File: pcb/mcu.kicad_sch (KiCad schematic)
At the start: 15 parts, among them J2 Conn_01x07_Pin, J3 62201021121, SW2 SKRKAEE020, SW3 SKRKAEE020, U2 MS88SF2

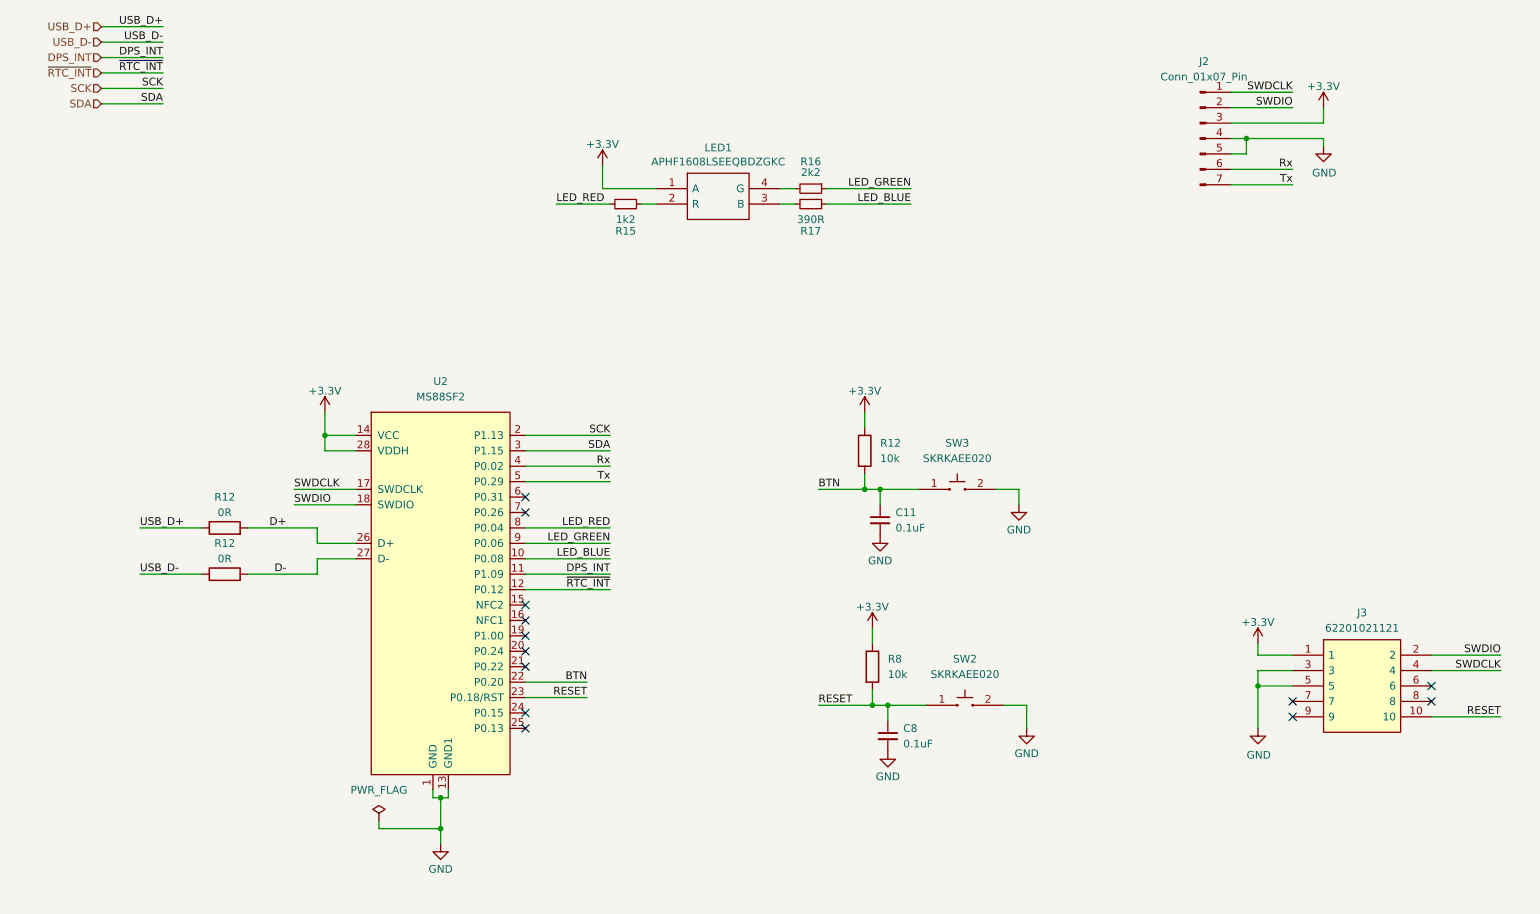
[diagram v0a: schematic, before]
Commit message: Replaces nRF52840 with ESP32-S3
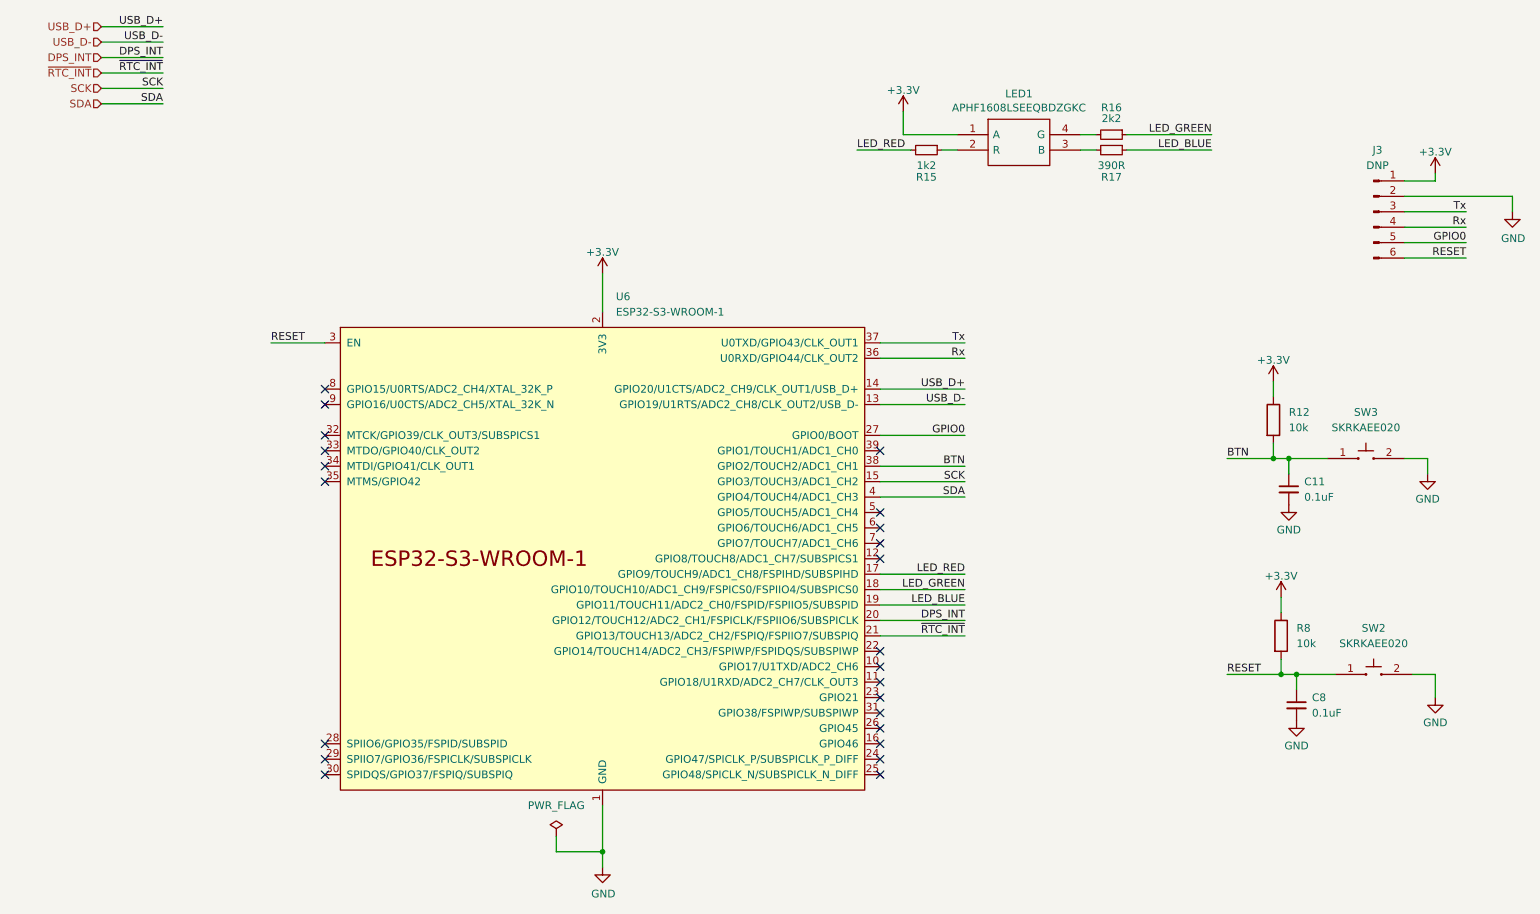
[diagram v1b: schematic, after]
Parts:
- removed J2: Conn_01x07_Pin, Connector_PinHeader_2.54mm:PinHeader_1x07_P2.54mm_Vertical, symbol Connector:Conn_01x07_Pin
- removed J3: 62201021121, 62201021121:WURTH-1.27MM-PITCH-2WAY, symbol 62201021121:62201021121
- removed R12 (x2): 0R, Resistor_SMD:R_0603_1608Metric, symbol Device:R
- removed U2: MS88SF2, MS88SF2:MS88SF2, symbol MS88SF2:MS88SF2
- added J3: DNP, Connector_PinSocket_2.54mm:PinSocket_1x06_P2.54mm_Vertical, symbol Connector:Conn_01x06_Pin
- added U6: ESP32-S3-WROOM-1, ESP32-S3:ESP32-S3-WROOM-1U, symbol Espressif:ESP32-S3-WROOM-1
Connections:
- net +3.3V: now also J3.1 (Pin_1), U6.2 (3V3)
- net BTN: now also U6.38 (GPIO2/TOUCH2/ADC1_CH1)
- net DPS_INT: now also U6.20 (GPIO12/TOUCH12/ADC2_CH1/FSPICLK/FSPIIO6/SUBSPICLK)
- net GND: now also J3.2 (Pin_2), U6.1 (GND), U6.40 (GND), U6.41 (GND)
- net LED_BLUE: now also U6.19 (GPIO11/TOUCH11/ADC2_CH0/FSPID/FSPIIO5/SUBSPID)
- net LED_GREEN: now also U6.18 (GPIO10/TOUCH10/ADC1_CH9/FSPICS0/FSPIIO4/SUBSPICS0)
- net LED_RED: now also U6.17 (GPIO9/TOUCH9/ADC1_CH8/FSPIHD/SUBSPIHD)
- net RESET: now also J3.6 (Pin_6), U6.3 (EN)
- net Rx: now also J3.4 (Pin_4), U6.36 (U0RXD/GPIO44/CLK_OUT2)
- net SCK: now also U6.15 (GPIO3/TOUCH3/ADC1_CH2)
- net SDA: now also U6.4 (GPIO4/TOUCH4/ADC1_CH3)
- net Tx: now also J3.3 (Pin_3), U6.37 (U0TXD/GPIO43/CLK_OUT1)
- net USB_D+: now also U6.14 (GPIO20/U1CTS/ADC2_CH9/CLK_OUT1/USB_D+)
- net USB_D-: now also U6.13 (GPIO19/U1RTS/ADC2_CH8/CLK_OUT2/USB_D-)
- net ~{RTC_INT}: now also U6.21 (GPIO13/TOUCH13/ADC2_CH2/FSPIQ/FSPIIO7/SUBSPIQ)
- new net GPIO0: J3.5 (Pin_5), U6.27 (GPIO0/BOOT)
- no-connect marks 13 -> 23
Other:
- moved on the sheet: C11, C8, LED1, R12, R15, R16, R17, R8, SW2, SW3

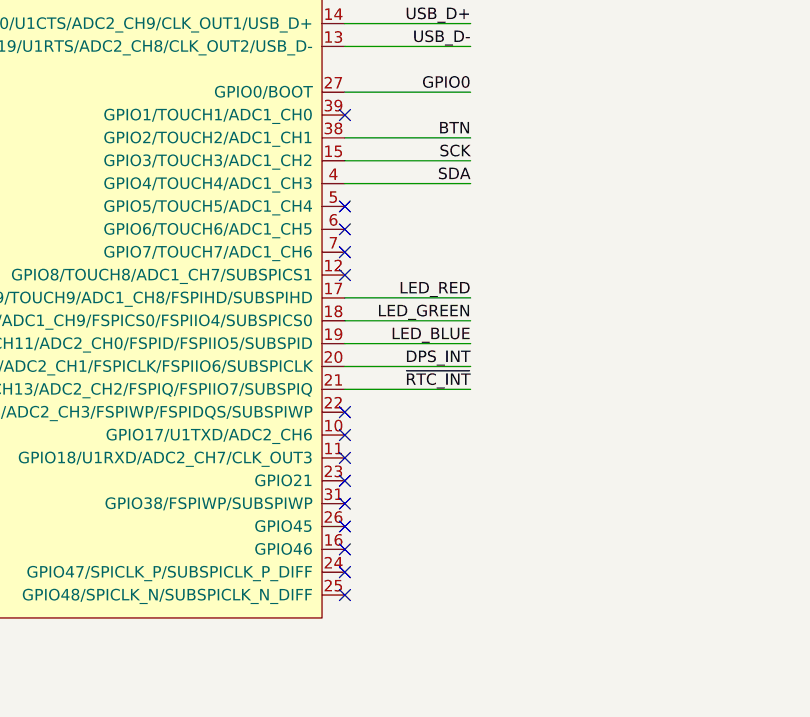
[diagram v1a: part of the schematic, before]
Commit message: Layout all components
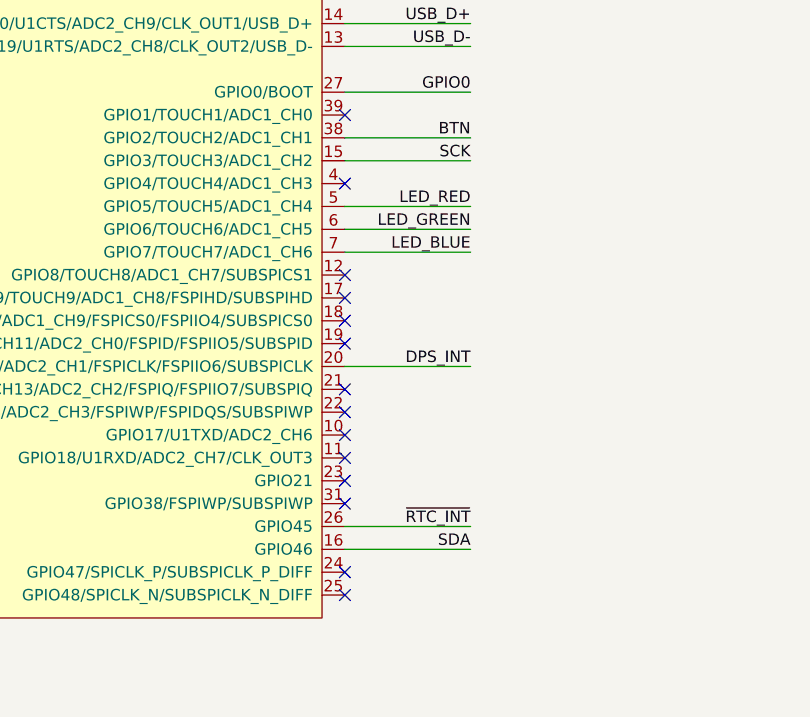
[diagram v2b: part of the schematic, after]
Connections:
- net LED_BLUE: now also U6.7 (GPIO7/TOUCH7/ADC1_CH6); no longer U6.19 (GPIO11/TOUCH11/ADC2_CH0/FSPID/FSPIIO5/SUBSPID)
- net LED_GREEN: now also U6.6 (GPIO6/TOUCH6/ADC1_CH5); no longer U6.18 (GPIO10/TOUCH10/ADC1_CH9/FSPICS0/FSPIIO4/SUBSPICS0)
- net LED_RED: now also U6.5 (GPIO5/TOUCH5/ADC1_CH4); no longer U6.17 (GPIO9/TOUCH9/ADC1_CH8/FSPIHD/SUBSPIHD)
- net SDA: now also U6.16 (GPIO46); no longer U6.4 (GPIO4/TOUCH4/ADC1_CH3)
- net ~{RTC_INT}: now also U6.26 (GPIO45); no longer U6.21 (GPIO13/TOUCH13/ADC2_CH2/FSPIQ/FSPIIO7/SUBSPIQ)
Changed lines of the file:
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@@
   (no_connect (at 154.94 129.54))
   (no_connect (at 63.5 139.7))
-  (no_connect (at 154.94 137.16))
   (no_connect (at 63.5 142.24))
   (no_connect (at 154.94 142.24))
   (no_connect (at 154.94 132.08))
+  (no_connect (at 154.94 96.52))
   (no_connect (at 154.94 124.46))
-  (no_connect (at 154.94 99.06))
+  (no_connect (at 154.94 119.38))
+  (no_connect (at 154.94 109.22))
   (no_connect (at 154.94 106.68))
-  (no_connect (at 154.94 101.6))
-  (no_connect (at 154.94 104.14))
+  (no_connect (at 154.94 111.76))
+  (no_connect (at 154.94 114.3))
   (no_connect (at 154.94 127))
   (no_connect (at 63.5 93.98))
   (no_connect (at 63.5 91.44))
-  (no_connect (at 154.94 134.62))
   (no_connect (at 63.5 78.74))
   (no_connect (at 63.5 88.9))
@@
     (stroke (width 0) (type default))
   )
-  (wire (pts (xy 168.91 111.76) (xy 154.94 111.76))
-    (stroke (width 0) (type default))
-  )
-  (wire (pts (xy 154.94 109.22) (xy 168.91 109.22))
+  (wire (pts (xy 168.91 101.6) (xy 154.94 101.6))
+    (stroke (width 0) (type default))
+  )
+  (wire (pts (xy 154.94 99.06) (xy 168.91 99.06))
     (stroke (width 0) (type default))
   )
@@
     (stroke (width 0) (type default))
   )
-  (wire (pts (xy 154.94 114.3) (xy 168.91 114.3))
+  (wire (pts (xy 154.94 104.14) (xy 168.91 104.14))
     (stroke (width 0) (type default))
   )
@@
     (stroke (width 0) (type default))
   )
-  (wire (pts (xy 154.94 96.52) (xy 168.91 96.52))
+  (wire (pts (xy 154.94 137.16) (xy 168.91 137.16))
     (stroke (width 0) (type default))
   )
@@
     (stroke (width 0) (type default))
   )
-  (wire (pts (xy 154.94 119.38) (xy 168.91 119.38))
+  (wire (pts (xy 154.94 134.62) (xy 168.91 134.62))
     (stroke (width 0) (type default))
   )
@@
     (stroke (width 0) (type default))
   )
-  (label "SDA" (at 168.91 96.52 180) (fields_autoplaced)
+  (label "SDA" (at 168.91 137.16 180) (fields_autoplaced)
     (effects (font (size 1.27 1.27)) (justify right bottom))
   )
@@
     (effects (font (size 1.27 1.27)) (justify left bottom))
   )
-  (label "LED_GREEN" (at 168.91 111.76 180) (fields_autoplaced)
+  (label "LED_GREEN" (at 168.91 101.6 180) (fields_autoplaced)
     (effects (font (size 1.27 1.27)) (justify right bottom))
   )
@@
     (effects (font (size 1.27 1.27)) (justify right bottom))
   )
-  (label "LED_RED" (at 168.91 109.22 180) (fields_autoplaced)
+  (label "LED_RED" (at 168.91 99.06 180) (fields_autoplaced)
     (effects (font (size 1.27 1.27)) (justify right bottom))
   )
@@
     (effects (font (size 1.27 1.27)) (justify right bottom))
   )
-  (label "LED_BLUE" (at 168.91 114.3 180) (fields_autoplaced)
+  (label "LED_BLUE" (at 168.91 104.14 180) (fields_autoplaced)
     (effects (font (size 1.27 1.27)) (justify right bottom))
   )
@@
     (effects (font (size 1.27 1.27)) (justify right bottom))
   )
-  (label "~{RTC_INT}" (at 168.91 119.38 180) (fields_autoplaced)
-    (effects (font (size 1.27 1.27)) (justify right bottom))
-  )
+  (label "~{RTC_INT}" (at 168.91 134.62 180) (fields_autoplaced)
+    (effects (font (size 1.27 1.27)) (justify right bottom))
+  )

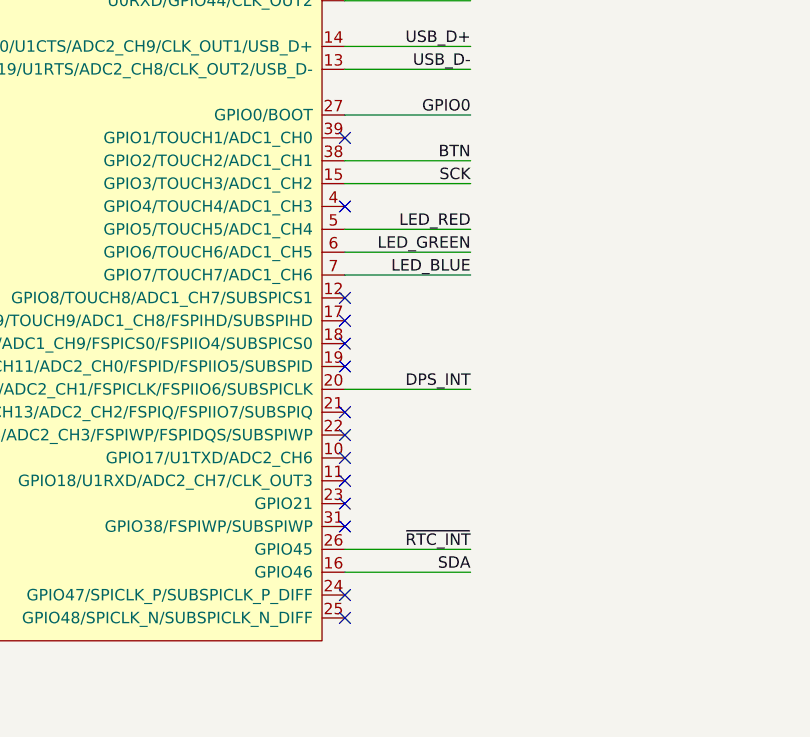
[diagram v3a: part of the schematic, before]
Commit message: Fixed usage of strapping pins
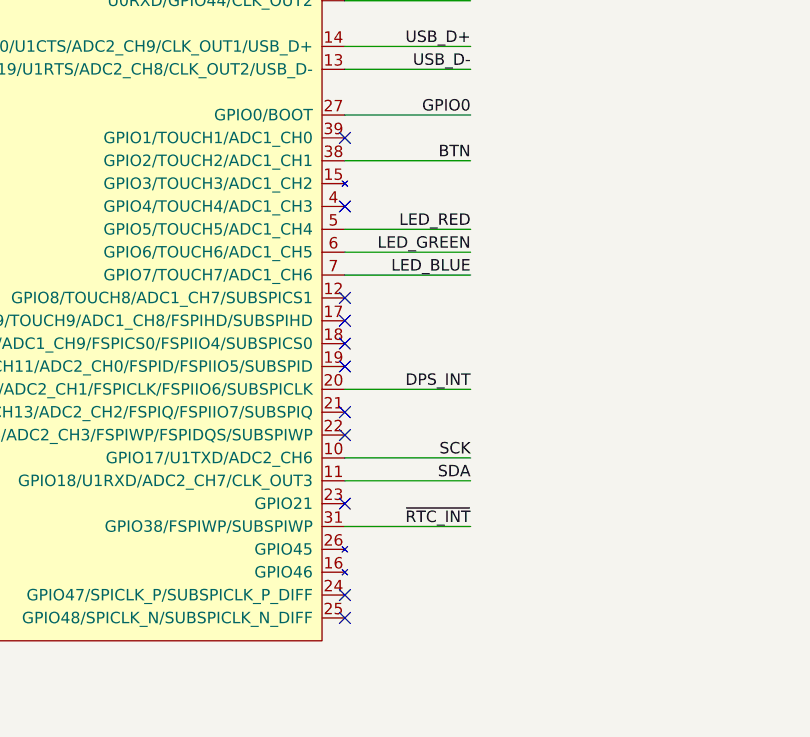
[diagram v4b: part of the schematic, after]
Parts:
- U6: footprint ESP32-S3:ESP32-S3-WROOM-1U -> PCM_Espressif:ESP32-S3-WROOM-1U
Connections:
- net SCK: now also U6.10 (GPIO17/U1TXD/ADC2_CH6); no longer U6.15 (GPIO3/TOUCH3/ADC1_CH2)
- net SDA: now also U6.11 (GPIO18/U1RXD/ADC2_CH7/CLK_OUT3); no longer U6.16 (GPIO46)
- net ~{RTC_INT}: now also U6.31 (GPIO38/FSPIWP/SUBSPIWP); no longer U6.26 (GPIO45)
- no-connect marks 23 -> 20
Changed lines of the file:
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@@
   (no_connect (at 63.5 142.24))
   (no_connect (at 154.94 142.24))
-  (no_connect (at 154.94 132.08))
   (no_connect (at 154.94 96.52))
-  (no_connect (at 154.94 124.46))
   (no_connect (at 154.94 119.38))
   (no_connect (at 154.94 109.22))
@@
   (no_connect (at 154.94 111.76))
   (no_connect (at 154.94 114.3))
-  (no_connect (at 154.94 127))
   (no_connect (at 63.5 93.98))
   (no_connect (at 63.5 91.44))
@@
     (stroke (width 0) (type default))
   )
-  (wire (pts (xy 154.94 137.16) (xy 168.91 137.16))
+  (wire (pts (xy 154.94 127) (xy 168.91 127))
     (stroke (width 0) (type default))
   )
@@
     (stroke (width 0) (type default))
   )
-  (wire (pts (xy 154.94 134.62) (xy 168.91 134.62))
+  (wire (pts (xy 154.94 132.08) (xy 168.91 132.08))
     (stroke (width 0) (type default))
   )
@@
     (stroke (width 0) (type default))
   )
-  (wire (pts (xy 154.94 93.98) (xy 168.91 93.98))
+  (wire (pts (xy 154.94 124.46) (xy 168.91 124.46))
     (stroke (width 0) (type default))
   )
@@
     (stroke (width 0) (type default))
   )
-  (label "SDA" (at 168.91 137.16 180) (fields_autoplaced)
+  (label "SDA" (at 168.91 127 180) (fields_autoplaced)
     (effects (font (size 1.27 1.27)) (justify right bottom))
   )
@@
     (effects (font (size 1.27 1.27)) (justify right bottom))
   )
-  (label "SCK" (at 168.91 93.98 180) (fields_autoplaced)
+  (label "SCK" (at 168.91 124.46 180) (fields_autoplaced)
     (effects (font (size 1.27 1.27)) (justify right bottom))
   )
@@
     (effects (font (size 1.27 1.27)) (justify right bottom))
   )
-  (label "~{RTC_INT}" (at 168.91 134.62 180) (fields_autoplaced)
+  (label "~{RTC_INT}" (at 168.91 132.08 180) (fields_autoplaced)
     (effects (font (size 1.27 1.27)) (justify right bottom))
   )
@@
       (effects (font (size 1.27 1.27)) (justify left))
     )
-    (property "Footprint" "ESP32-S3:ESP32-S3-WROOM-1U" (at 111.76 154.94 0)
+    (property "Footprint" "PCM_Espressif:ESP32-S3-WROOM-1U" (at 111.76 154.94 0)
       (effects (font (size 1.27 1.27)) hide)
     )
@@
     (pin "13")
     (pin "14")
-    (pin "15")
-    (pin "16")
     (pin "17")
     (pin "18")
@@
     (pin "24")
     (pin "25")
-    (pin "26")
     (pin "27")
     (pin "28")
@@
     (pin "8")
     (pin "9")
-    (instances
-      (project "ot-riwa"
+    (pin "15")
+    (pin "16")
+    (pin "26")
+    (instances
+      (project "ot-riwa"
